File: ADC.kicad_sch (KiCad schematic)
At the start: 164 parts, among them J1 Conn_01x03_Pin, J2 Screw_Terminal_01x02, J3 Screw_Terminal_01x09, SW1 SW_SPDT, U1 ADS1256IDBR, U10 CD4514BM, U11 ADG5412FBCPZ-RL7, U12 ADR421ARMZ, U13 OPA211ID, U14 ADG5412FBCPZ-RL7, U15 OPA211ID, U16 ADG5412FBCPZ-RL7, U17 OPA211ID, U18 CD4072BM, U19 CD4514BM, U2 MCU-STM32F407VET6_LQFP100_, U20 ADG5412FBCPZ-RL7, U21 ADG5412FBCPZ-RL7, U22 ADG5412FBCPZ-RL7, U23 ADG5412FBCPZ-RL7, U24 OPA211ID, U25 OPA211ID, U26 OPA211ID, U27 OPA211ID, U3 ADM2483xRW, U4 LM2596S-5, U5 DCP010505BP, U6 TLV1704AIPWR, U7 OPA211ID, U8 AMS1117-3.3, U9 ADG5412FBCPZ-RL7, Y1 8MHz, Y2 ABM3B-25.000MHZ-D2Y-T

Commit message: Them Cd
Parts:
- added U28: CD4043BPWR, CD4043BPWR:SOP65P640X120-16N, symbol CD4043BPWR:CD4043BPWR
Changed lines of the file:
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@@
+	)
+	(symbol
+		(lib_id "CD4043BPWR:CD4043BPWR")
+		(at 163.83 618.49 0)
+		(unit 1)
+		(exclude_from_sim no)
+		(in_bom yes)
+		(on_board yes)
+		(dnp no)
+		(fields_autoplaced yes)
+		(property "Reference" "U28"
+			(at 163.83 593.09 0)
+			(effects
+				(font
+					(size 1.27 1.27)
+				)
+			)
+		)
+		(property "Value" "CD4043BPWR"
+			(at 163.83 595.63 0)
+			(effects
+				(font
+					(size 1.27 1.27)
+				)
+			)
+		)
+		(property "Footprint" "CD4043BPWR:SOP65P640X120-16N"
+			(at 163.83 618.49 0)
+			(effects
+				(font
+					(size 1.27 1.27)
+				)
+				(justify bottom)
+				(hide yes)
+			)
+		)
+		(property "Datasheet" ""
+			(at 163.83 618.49 0)
+			(effects
+				(font
+					(size 1.27 1.27)
+				)
+				(hide yes)
+			)
+		)
+		(property "Description" ""
+			(at 163.83 618.49 0)
+			(effects
+				(font
+					(size 1.27 1.27)
+				)
+				(hide yes)
+			)
+		)
+		(property "MF" "Texas Instruments"
+			(at 163.83 618.49 0)
+			(effects
+				(font
+					(size 1.27 1.27)
+				)
+				(justify bottom)
+				(hide yes)
+			)
+		)
+		(property "Description_1" "\n                        \n                            CMOS Quad NOR R/S Latch with 3-State Outputs\n                        \n"
+			(at 163.83 618.49 0)
+			(effects
+				(font
+					(size 1.27 1.27)
+				)
+				(justify bottom)
+				(hide yes)
+			)
+		)
+		(property "Package" "TSSOP-16 Texas Instruments"
+			(at 163.83 618.49 0)
+			(effects
+				(font
+					(size 1.27 1.27)
+				)
+				(justify bottom)
+				(hide yes)
+			)
+		)
+		(property "Price" "None"
+			(at 163.83 618.49 0)
+			(effects
+				(font
+					(size 1.27 1.27)
+				)
+				(justify bottom)
+				(hide yes)
+			)
+		)
+		(property "SnapEDA_Link" "https://www.snapeda.com/parts/CD4043BPWR/Texas+Instruments/view-part/?ref=snap"
+			(at 163.83 618.49 0)
+			(effects
+				(font
+					(size 1.27 1.27)
+				)
+				(justify bottom)
+				(hide yes)
+			)
+		)
+		(property "MP" "CD4043BPWR"
+			(at 163.83 618.49 0)
+			(effects
+				(font
+					(size 1.27 1.27)
+				)
+				(justify bottom)
+				(hide yes)
+			)
+		)
+		(property "Availability" "In Stock"
+			(at 163.83 618.49 0)
+			(effects
+				(font
+					(size 1.27 1.27)
+				)
+				(justify bottom)
+				(hide yes)
+			)
+		)
+		(property "Check_prices" "https://www.snapeda.com/parts/CD4043BPWR/Texas+Instruments/view-part/?ref=eda"
+			(at 163.83 618.49 0)
+			(effects
+				(font
+					(size 1.27 1.27)
+				)
+				(justify bottom)
+				(hide yes)
+			)
+		)
+		(pin "11"
+		)
+		(pin "5"
+		)
+		(pin "14"
+		)
+		(pin "7"
+		)
+		(pin "16"
+		)
+		(pin "4"
+		)
+		(pin "9"
+		)
+		(pin "1"
+		)
+		(pin "15"
+		)
+		(pin "8"
+		)
+		(pin "2"
+		)
+		(pin "3"
+		)
+		(pin "12"
+		)
+		(pin "10"
+		)
+		(pin "6"
+		)
+		(instances
+			(project ""
+				(path "/c7ceee6a-ba62-44b0-b5ba-f64f163625fc"
+					(reference "U28")
+					(unit 1)
+				)
+			)
+		)
 	)
 	(symbol

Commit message: hoàn thành bảo vệ ADC
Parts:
- added R71, R72, R73, R74, R79, R80, R81, R82, R83, R84, R85, R86, R87, R88, R89, R90: 3k, symbol Device:R
- added R75, R78: 2k, symbol Device:R
- added R76, R77: 1k, symbol Device:R
- added U29, U30, U31: TLV1704AIPWR, TLV1704AIPWR:SOP65P640X120-14N, symbol TLV1704AIPWR:TLV1704AIPWR
- added U32: CD4072BM, CD4072BM:SOIC127P600X175-14N, symbol CD4072BM:CD4072BM
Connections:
- net +12V: now also U6.3 (V+), R75.1, U29.3 (V+), U30.3 (V+), U31.3 (V+)
- net +3.3V: now also U18.14 (VDD), U28.16 (VDD), U28.5 (ENABLE), R71.1, R72.1, R73.1, R74.2, R79.2, R80.1, R81.1, R82.1, R83.2, R84.2, R85.1, R86.1, R87.1, R88.1, R89.1, R90.1, U32.14 (VDD)
- net -12V: now also U6.12 (V_), R78.2, U29.12 (V_), U30.12 (V_), U31.12 (V_)
- net ADC1: now also U6.5 (1IN+), U6.6 (2LN-)
- net ADC2: now also U6.10 (4IN-), U6.9 (3LN+)
- net ADC3: now also U29.5 (1IN+), U29.6 (2LN-)
- net ADC4: now also U29.10 (4IN-), U29.9 (3LN+)
- net ADC5: now also U30.5 (1IN+), U30.6 (2LN-)
- net ADC6: now also U30.10 (4IN-), U30.9 (3LN+)
- net ADC7: now also U31.5 (1IN+), U31.6 (2LN-)
- net ADC8: now also U31.10 (4IN-), U31.9 (3LN+)
- net DECODER1_1: now also U2.17 (PC2); no longer U2.15 (PC0)
- net DECODER1_2: now also U2.18 (PC3); no longer U2.16 (PC1)
- net DECODER1_3: now also U2.33 (PC4); no longer U2.17 (PC2)
- net DECODER1_4: now also U2.34 (PC5); no longer U2.18 (PC3)
- net DECODER2_1: now also U2.64 (PC7); no longer U2.63 (PC6)
- net DECODER2_2: now also U2.65 (PC8); no longer U2.64 (PC7)
- net DECODER2_3: now also U2.66 (PC9); no longer U2.65 (PC8)
- net DECODER2_4: now also U2.78 (PC10); no longer U2.66 (PC9)
- net GND: now also U18.7 (VSS), U28.8 (VSS), R76.2, R77.1, U32.7 (VSS)
- net LOCK4: now reaches U28.1 (Q4)
- net LOCK4: now also U19.1 (STROBE)
- net LOCK3: now reaches U28.10 (Q3)
- net LOCK3: now also U19.23 (INHIBIT)
- net RESET: now reaches U28.11 (R3)
- net RESET: now also U2.15 (PC0), U28.15 (R4), U28.3 (R1), U28.7 (R2)
- net at U28.12 (S3): now also U32.1 (J=A+B+C+D)
- net at U28.14 (S4): now also U32.13 (K=E+F+G+H)
- net LOCK1: now reaches U28.2 (Q1)
- net LOCK1: now also U10.23 (INHIBIT)
- net at U28.4 (S1): now also U18.1 (J=A+B+C+D)
- net at U28.6 (S2): now also U18.13 (K=E+F+G+H)
- net LOCK2: now reaches U28.9 (Q2)
- net LOCK2: now also U10.1 (STROBE)
- net at U6.1 (20UT): now also U18.4 (C), R72.2
- net -4V: now reaches U6.11 (4IN+)
- net -4V: now also U6.7 (2LN+), R77.2, R78.1, U29.11 (4IN+), U29.7 (2LN+), U30.11 (4IN+), U30.7 (2LN+), U31.11 (4IN+), U31.7 (2LN+)
- net at U6.13 (40UT): now also U18.2 (A), R74.1
- net at U6.14 (30UT): now also U18.3 (B), R73.2
- net at U6.2 (10UT): now also U18.5 (D), R71.2
- net +4V: now reaches U6.4 (1IN-)
- net +4V: now also U6.8 (3LN-), R75.2, R76.1, U29.4 (1IN-), U29.8 (3LN-), U30.4 (1IN-), U30.8 (3LN-), U31.4 (1IN-), U31.8 (3LN-)
- net at U18.10 (F): now also R80.2, U29.14 (30UT)
- net at U18.11 (G): now also R81.2, U29.1 (20UT)
- net at U18.12 (H): now also R82.2, U29.2 (10UT)
- net at U18.9 (E): now also R79.1, U29.13 (40UT)
- removed net DECODER1_5: U10.23 (INHIBIT), U2.33 (PC4)
- removed net DECODER1_6: U10.1 (STROBE), U2.34 (PC5)
- removed net DECODER2_5: U19.23 (INHIBIT), U2.78 (PC10)
- net DECODER2_6: no longer names the net of U2.79 (PC11)
- net DECODER2_6: no longer U19.1 (STROBE)
- new net: R87.2, U30.1 (20UT), U32.4 (C)
- new net: R86.2, U31.14 (30UT), U32.10 (F)
- new net: R88.2, U31.1 (20UT), U32.11 (G)
- new net: R84.1, U31.13 (40UT), U32.9 (E)
- new net: R90.2, U31.2 (10UT), U32.12 (H)
- new net: R85.2, U30.14 (30UT), U32.3 (B)
- new net: R83.1, U30.13 (40UT), U32.2 (A)
- new net: R89.2, U30.2 (10UT), U32.5 (D)
- no-connect marks 78 -> 81
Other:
- moved on the sheet: D10, D11, D12, D13, D14, D7, D8, D9, J3, R1, R25, R26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

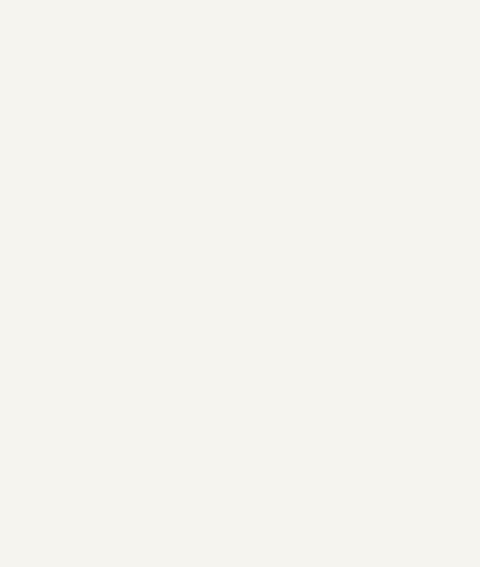
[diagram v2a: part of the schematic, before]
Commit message: Add SMDJ
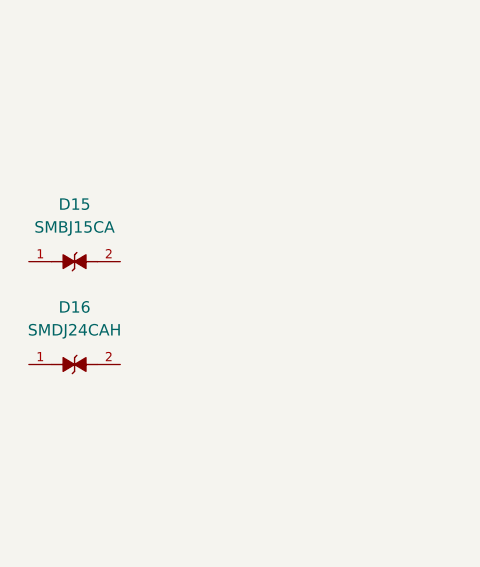
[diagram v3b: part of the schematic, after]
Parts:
- added D15: SMBJ15CA, SMBJ15CA:DIOM4336X265N, symbol SMBJ15CA:SMBJ15CA
- added D16: SMDJ24CAH, SMDJ24CAH:DIOM6859X262N, symbol SMDJ24CAH:SMDJ24CAH

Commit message: hoàn thiện
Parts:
- removed D10, D11, D12, D13, D14, D6, D7, D8, D9: D_TVS_Filled, symbol Device:D_TVS_Filled
- added D10, D11, D12, D13, D14, D19, D21, D23, D7, D8, D9: SMBJ15CA, SMBJ15CA:DIOM4336X265N, symbol SMBJ15CA:SMBJ15CA
- added D17, D6: SMDJ24CAH, SMDJ24CAH:DIOM6859X262N, symbol SMDJ24CAH:SMDJ24CAH
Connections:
- net GND: now also D15.2, D10.2, D11.2, D12.2, D13.2, D17.2, D7.2, D8.2, D9.2
- net GND_ISO: now also D16.2, D6.2
- net VinN1: now also D14.2, D7.1
- net VinN2: now also D19.2, D9.1
- net VinN3: now also D11.1, D21.2
- net VinN4: now also D13.1, D23.2
- net VinP1: now also D15.1, D14.1
- net VinP2: now also D19.1, D8.1
- net VinP3: now also D10.1, D21.1
- net VinP4: now also D12.1, D23.1
- net at D16.1: now also D4.1 (K), J1.3 (Pin_3), R21.2
- net at D1.1 (K), F1.2, L2.1: now also D17.1
- net at D5.1 (K), J1.2 (Pin_2), R22.2: now also D6.1
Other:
- moved on the sheet: D15, D5, J1, J3

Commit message: Add footprint, 3d
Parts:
- C1: footprint (none) -> Capacitor_THT:C_Radial_D8.0mm_H7.0mm_P3.50mm
- C10, C11, C23, C7: footprint (none) -> Capacitor_SMD:C_0805_2012Metric
- C13, C20, C35, C39, C40, C9: footprint (none) -> Capacitor_SMD:C_0603_1608Metric
- C17, C18, C19, C21, C22, C24, C25, C26, C27, C31, C33, C34, C38, C41: footprint (none) -> Capacitor_SMD:C_0402_1005Metric
- C32: footprint Capacitor_SMD:C_0603_1608Metric -> Capacitor_SMD:C_0402_1005Metric
- C43, C44: footprint Capacitor_SMD:C_0402_1005Metric -> Capacitor_THT:C_Radial_D8.0mm_H11.5mm_P3.50mm
- D1, D3: footprint (none) -> Diode_SMD:D_0805_2012Metric
- D2: footprint (none) -> LED_SMD:LED_0603_1608Metric
- D4, D5: footprint Diode_THT:D_DO-35_SOD27_P10.16mm_Horizontal -> Diode_THT:D_DO-35_SOD27_P7.62mm_Horizontal
- F1: footprint (none) -> Fuse:Fuse_1812_4532Metric
- J1: footprint (none) -> Connector_PinHeader_2.54mm:PinHeader_1x03_P2.54mm_Vertical
- J2: footprint (none) -> TerminalBlock:TerminalBlock_Altech_AK300-2_P5.00mm
- J3: footprint (none) -> TerminalBlock_Altech:Altech_AK100_1x09_P5.00mm
- L1, L2: footprint (none) -> Inductor_SMD:L_0603_1608Metric
- R1, R10, R11, R12, R13, R14, R15, R16, R17, R18, R19, R2, R20, R21, R22, R24, R25, R26, R27, R28, R29, R3, R30, R31, R32, R33, R34, R35, R36, R37, R38, R39, R4, R40, R41, R42, R43, R44, R45, R46, R47, R48, R49, R5, R50, R51, R52, R53, R54, R55, R56, R57, R58, R59, R6, R60, R61, R62, R63, R64, R65, R66, R67, R68, R69, R7, R70, R71, R72, R73, R74, R75, R76, R77, R78, R79, R8, R80, R81, R82, R83, R84, R85, R86, R87, R88, R89, R9, R90: footprint (none) -> Resistor_SMD:R_0402_1005Metric
- RV1: footprint (none) -> Varistor:RV_Disc_D7mm_W4.5mm_P5mm
- SW1: footprint Button_Switch_THT:SW_E-Switch_EG1224_SPDT_Angled -> Button_Switch_SMD:Nidec_Copal_CAS-120A
- U4: footprint Package_TO_SOT_SMD:TO-263-5_TabPin3 -> LM2596S-5.0:TO170P1524X483-6N
- U5: footprint DCP010505BP:DIP254P762X533-7P -> DCP10505BP:DIP254P762X533-7P
- Y1: footprint (none) -> Crystal:Crystal_HC49-4H_Vertical

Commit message: add 3d
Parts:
- J2: footprint TerminalBlock:TerminalBlock_Altech_AK300-2_P5.00mm -> TerminalBlock_Phoenix:TerminalBlock_Phoenix_MKDS-1,5-2_1x02_P5.00mm_Horizontal
- J3: footprint TerminalBlock_Altech:Altech_AK100_1x09_P5.00mm -> TerminalBlock_Phoenix:TerminalBlock_Phoenix_MPT-0,5-9-2.54_1x09_P2.54mm_Horizontal
- SW1: footprint Button_Switch_SMD:Nidec_Copal_CAS-120A -> Button_Switch_SMD:SW_SPDT_PCM12
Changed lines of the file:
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@@
 			)
 		)
-		(property "Footprint" "Button_Switch_SMD:Nidec_Copal_CAS-120A"
+		(property "Footprint" "Button_Switch_SMD:SW_SPDT_PCM12"
 			(at 989.33 527.05 0)
 			(effects
@@
 			)
 		)
-		(property "Footprint" "TerminalBlock:TerminalBlock_Altech_AK300-2_P5.00mm"
+		(property "Footprint" "TerminalBlock_Phoenix:TerminalBlock_Phoenix_MKDS-1,5-2_1x02_P5.00mm_Horizontal"
 			(at 307.34 83.82 0)
 			(effects
@@
 			)
 		)
-		(property "Footprint" "TerminalBlock_Altech:Altech_AK100_1x09_P5.00mm"
+		(property "Footprint" "TerminalBlock_Phoenix:TerminalBlock_Phoenix_MPT-0,5-9-2.54_1x09_P2.54mm_Horizontal"
 			(at 154.94 114.3 0)
 			(effects

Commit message: chia khu linh kiện PCB
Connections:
- net VinP5 is gone; now on net VinP3: U26.3 (+IN)
- net VinP6 is gone; now on net VinN3: U27.3 (+IN)
- net VinP7 is gone; now on net VinP4: U24.3 (+IN)
- net VinP8 is gone; now on net VinN4: U25.3 (+IN)
- net DECODER1_1: now also U2.57 (PD10); no longer U2.17 (PC2)
- net DECODER1_2: now also U2.58 (PD11); no longer U2.18 (PC3)
- net DECODER1_3: now also U2.59 (PD12); no longer U2.33 (PC4)
- net DECODER1_4: now also U2.60 (PD13); no longer U2.34 (PC5)
- net DECODER2_1: now also U2.63 (PC6); no longer U2.64 (PC7)
- net DECODER2_2: now also U2.64 (PC7); no longer U2.65 (PC8)
- net DECODER2_3: now also U2.65 (PC8); no longer U2.66 (PC9)
- net DECODER2_4: now also U2.66 (PC9); no longer U2.78 (PC10)
- net GND: now also J3.1 (Pin_1); no longer J3.9 (Pin_9)
- net RESET: now also U2.62 (PD15); no longer U2.15 (PC0)
- net VinN1: now also D12.1, D23.2, J3.3 (Pin_3), U13.3 (+IN); no longer D14.2, D7.1, J3.2 (Pin_2)
- net VinN2: now also D10.1, D21.2, J3.5 (Pin_5), U17.3 (+IN); no longer D19.2, D9.1, J3.4 (Pin_4)
- net VinN3: now also D19.2, D8.1, J3.7 (Pin_7); no longer D11.1, D21.2, J3.6 (Pin_6)
- net VinN4: now also D14.2, D15.1, J3.9 (Pin_9); no longer D13.1, D23.2, J3.8 (Pin_8)
- net VinP1: now also D13.1, D23.1, J3.2 (Pin_2); no longer D14.1, D15.1, J3.1 (Pin_1)
- net VinP2: now also D11.1, D21.1, J3.4 (Pin_4), U15.3 (+IN); no longer D19.1, D8.1, J3.3 (Pin_3), U13.3 (+IN)
- net VinP3: now also D19.1, D9.1, J3.6 (Pin_6); no longer D10.1, D21.1, J3.5 (Pin_5), U15.3 (+IN)
- net VinP4: now also D14.1, D7.1, J3.8 (Pin_8); no longer D12.1, D23.1, J3.7 (Pin_7), U17.3 (+IN)

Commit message: update
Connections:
- net 1_IN2: now reaches U9.14 (IN2)
- net 1_IN2: now also U10.4 (S7); no longer U10.10 (S1)
- net 1_IN1: now reaches U9.15 (IN1)
- net 1_IN1: now also U10.5 (S6); no longer U10.11 (S0)
- net 3_IN2: now reaches U10.13 (S13)
- net 3_IN2: now also U14.14 (IN2); no longer U16.14 (IN2)
- net 3_IN1: now reaches U10.14 (S12)
- net 3_IN1: now also U14.15 (IN1); no longer U16.15 (IN1)
- net 3_IN4: now reaches U10.15 (S15)
- net 3_IN4: now also U14.6 (IN4); no longer U16.6 (IN4)
- net 3_IN3: now reaches U10.16 (S14)
- net 3_IN3: now also U14.7 (IN3); no longer U16.7 (IN3)
- net 4_IN2: now reaches U10.17 (S9)
- net 4_IN2: now also U16.14 (IN2); no longer U14.14 (IN2)
- net 4_IN1: now reaches U10.18 (S8)
- net 4_IN1: now also U16.15 (IN1); no longer U14.15 (IN1)
- net 4_IN4: now reaches U10.19 (S11)
- net 4_IN4: now also U16.6 (IN4); no longer U14.6 (IN4)
- net 4_IN3: now reaches U10.20 (S10)
- net 4_IN3: now also U16.7 (IN3); no longer U14.7 (IN3)
- net 2_IN4: now reaches U11.6 (IN4)
- net 2_IN4: now also U10.10 (S1); no longer U10.4 (S7)
- net 2_in3: now reaches U11.7 (IN3)
- net 2_in3: now also U10.11 (S0); no longer U10.5 (S6)
- net 1_IN4: now reaches U10.6 (S5)
- net 1_IN4: now also U9.6 (IN4); no longer U11.14 (IN2)
- net 1_IN3: now reaches U10.7 (S4)
- net 1_IN3: now also U9.7 (IN3); no longer U11.15 (IN1)
- net 2_IN2: now reaches U10.8 (S3)
- net 2_IN2: now also U11.14 (IN2); no longer U9.6 (IN4)
- net 2_IN1: now reaches U10.9 (S2)
- net 2_IN1: now also U11.15 (IN1); no longer U9.7 (IN3)
